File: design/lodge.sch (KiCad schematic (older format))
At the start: 12 parts

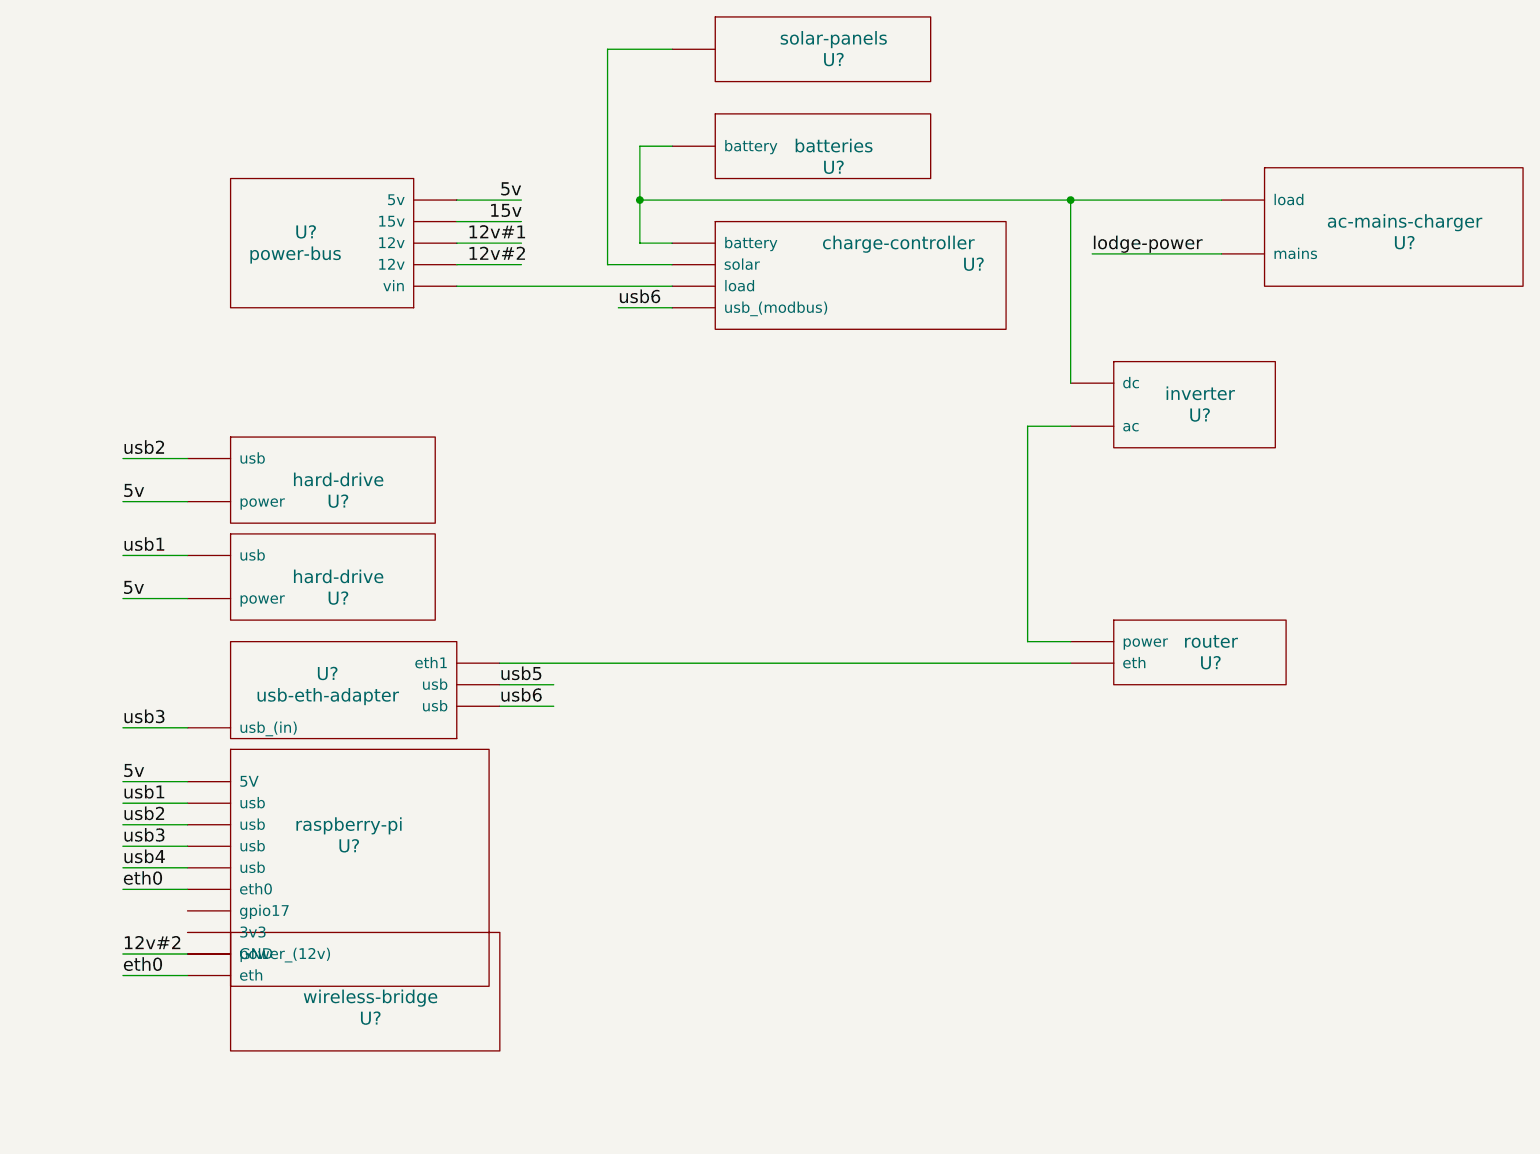
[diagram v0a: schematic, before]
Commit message: Hide component references.
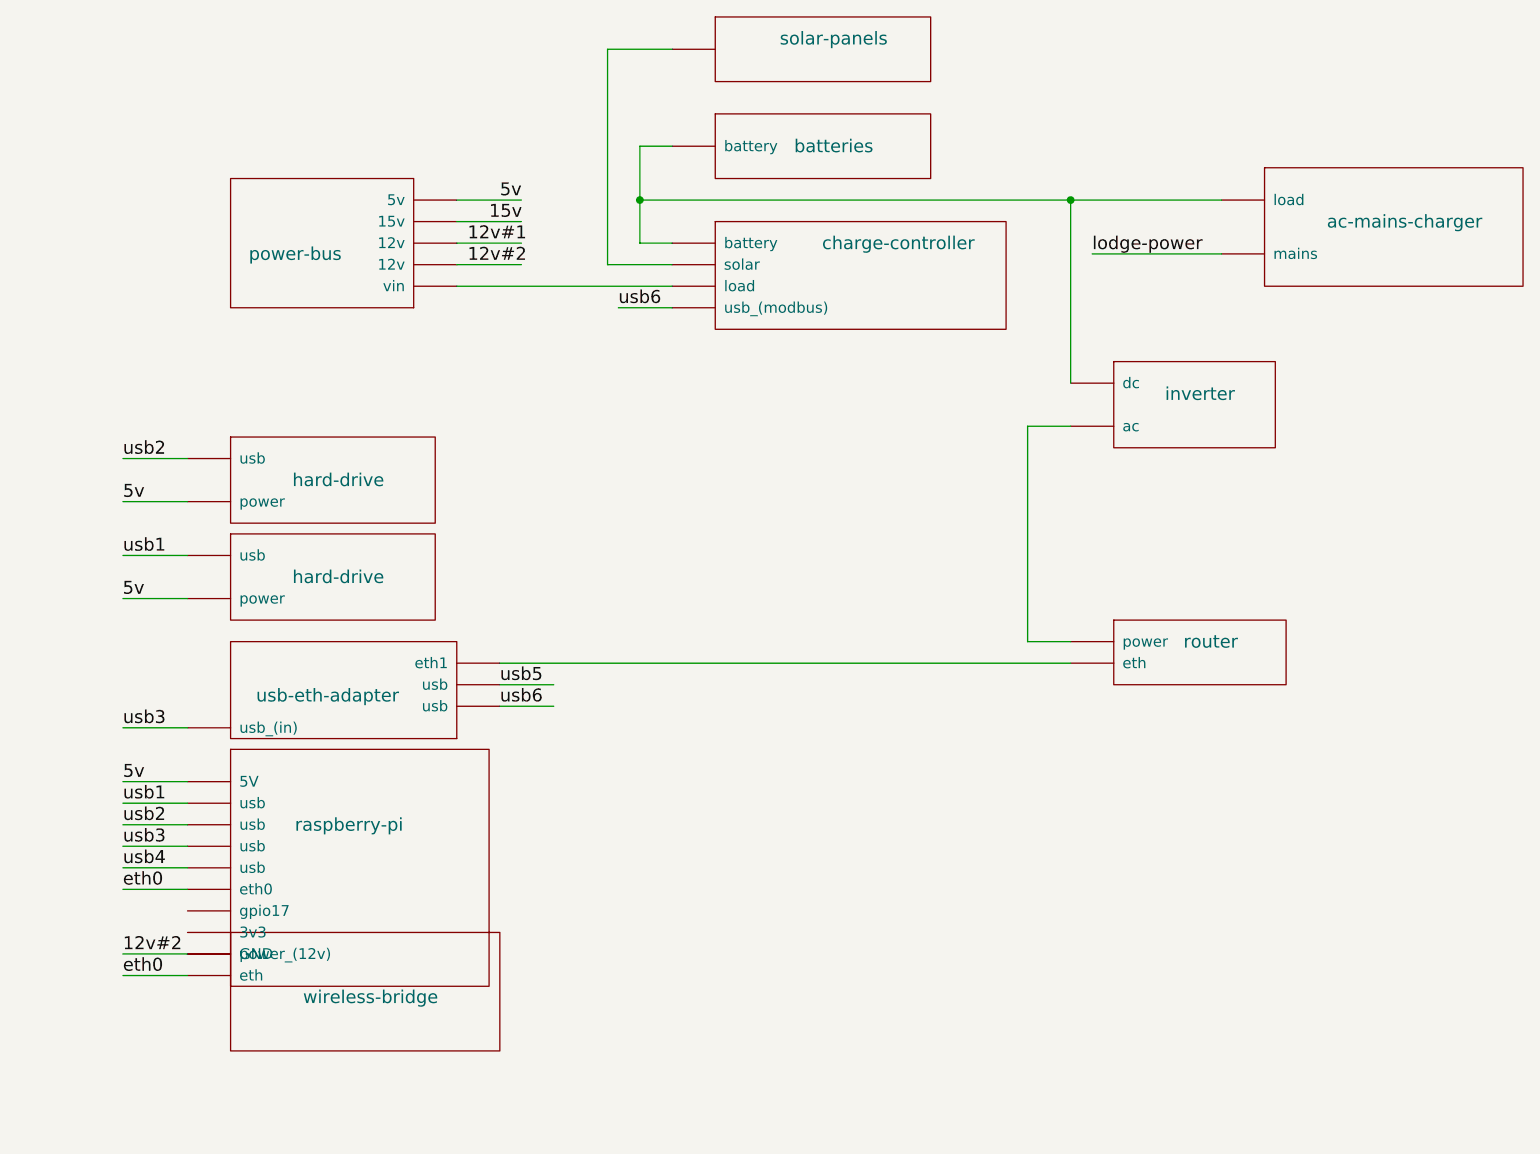
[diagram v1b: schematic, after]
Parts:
- gave numbers to parts that had none: 12
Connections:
- wire segments 36 -> 34
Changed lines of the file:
@@
 LIBS:valves
 LIBS:high-level
+LIBS:design-cache
 EELAYER 25 0
 EELAYER END
@@
 $EndDescr
 $Comp
-L charge-controller U?
+L charge-controller U23
 U 1 1 593F5FDD
 P 6750 2600
-F 0 "U?" H 6900 2700 60  0000 C CNN
+F 0 "U23" H 6900 2700 60  0001 C CNN
 F 1 "charge-controller" H 6550 2800 60  0000 C CNN
 F 2 "" H 6750 2600 60  0001 C CNN
@@
 $EndComp
 $Comp
-L power-bus U?
+L power-bus U15
 U 1 1 593F5FEB
 P 3750 2450
-F 0 "U?" H 3700 2350 60  0000 C CNN
+F 0 "U15" H 3700 2350 60  0001 C CNN
 F 1 "power-bus" H 3750 2450 60  0000 C CNN
 F 2 "" H 3750 2450 60  0001 C CNN
@@
 $EndComp
 $Comp
-L raspberry-pi U?
+L raspberry-pi U19
 U 1 1 593F5FF2
 P 4000 5100
-F 0 "U?" H 4000 5000 60  0000 C CNN
+F 0 "U19" H 4000 5000 60  0001 C CNN
 F 1 "raspberry-pi" H 4000 5100 60  0000 C CNN
 F 2 "" H 4000 5100 60  0001 C CNN
@@
 $EndComp
 $Comp
-L usb-eth-adapter U?
+L usb-eth-adapter U16
 U 1 1 593F5FF9
 P 3900 4500
-F 0 "U?" H 3900 4400 60  0000 C CNN
+F 0 "U16" H 3900 4400 60  0001 C CNN
 F 1 "usb-eth-adapter" H 3900 4500 60  0000 C CNN
 F 2 "" H 3900 4500 60  0001 C CNN
@@
 $EndComp
 $Comp
-L wireless-bridge U?
+L wireless-bridge U20
 U 1 1 593F6000
 P 4100 5900
-F 0 "U?" H 4100 5800 60  0000 C CNN
+F 0 "U20" H 4100 5800 60  0001 C CNN
 F 1 "wireless-bridge" H 4100 5900 60  0000 C CNN
 F 2 "" H 4100 5900 60  0001 C CNN
@@
 $EndComp
 $Comp
-L hard-drive U?
+L hard-drive U18
 U 1 1 593F6007
 P 3950 3950
-F 0 "U?" H 3950 3850 60  0000 C CNN
+F 0 "U18" H 3950 3850 60  0001 C CNN
 F 1 "hard-drive" H 3950 3950 60  0000 C CNN
 F 2 "" H 3950 3950 60  0001 C CNN
@@
 $EndComp
 $Comp
-L hard-drive U?
+L hard-drive U17
 U 1 1 593F600E
 P 3950 3500
-F 0 "U?" H 3950 3400 60  0000 C CNN
+F 0 "U17" H 3950 3400 60  0001 C CNN
 F 1 "hard-drive" H 3950 3500 60  0000 C CNN
 F 2 "" H 3950 3500 60  0001 C CNN
@@
 12v#2
 $Comp
-L batteries U?
+L batteries U22
 U 1 1 593F601A
 P 6250 1950
-F 0 "U?" H 6250 1850 60  0000 C CNN
+F 0 "U22" H 6250 1850 60  0001 C CNN
 F 1 "batteries" H 6250 1950 60  0000 C CNN
 F 2 "" H 6250 1950 60  0001 C CNN
@@
 	5350 2400 5500 2400
 Wire Wire Line
-	5350 1950 5350 2200
-Wire Wire Line
-	5350 2200 5350 2400
+	5350 1950 5350 2400
 Wire Wire Line
 	5350 1950 5500 1950
@@
 	5250 2700 5500 2700
 $Comp
-L solar-panels U?
+L solar-panels U21
 U 1 1 593F606C
 P 6250 1500
-F 0 "U?" H 6250 1450 60  0000 C CNN
+F 0 "U21" H 6250 1450 60  0001 C CNN
 F 1 "solar-panels" H 6250 1550 60  0000 C CNN
 F 2 "" H 6250 1550 60  0001 C CNN
@@
 	5200 1500 5500 1500
 $Comp
-L ac-mains-charger U?
+L ac-mains-charger U26
 U 1 1 593F63BD
 P 8900 2300
-F 0 "U?" H 8900 2200 60  0000 C CNN
+F 0 "U26" H 8900 2200 60  0001 C CNN
 F 1 "ac-mains-charger" H 8900 2300 60  0000 C CNN
 F 2 "" H 8900 2300 60  0001 C CNN
@@
 $EndComp
 $Comp
-L inverter U?
+L inverter U24
 U 1 1 593F6430
 P 7950 3150
-F 0 "U?" H 7950 3100 60  0000 C CNN
+F 0 "U24" H 7950 3100 60  0001 C CNN
 F 1 "inverter" H 7950 3200 60  0000 C CNN
 F 2 "" H 7950 3200 60  0001 C CNN
@@
 $EndComp
 $Comp
-L router U?
+L router U25
 U 1 1 593F66CA
 P 8000 4300
-F 0 "U?" H 8000 4250 60  0000 C CNN
+F 0 "U25" H 8000 4250 60  0001 C CNN
 F 1 "router" H 8000 4350 60  0000 C CNN
 F 2 "" H 8000 4350 60  0001 C CNN
@@
 $EndComp
 Wire Wire Line
-	5350 2200 7350 2200
-Wire Wire Line
-	7350 2200 8050 2200
+	5350 2200 8050 2200
 Wire Wire Line
 	7350 2200 7350 3050

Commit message: Updating hardware design docs.
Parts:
- removed U17: hard-drive, symbol hard-drive
- added U?: relay-board, symbol relay-board
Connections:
- net labels added: +3V3, GND, relay_en
- net labels removed: 12v#1, 15v
- wire segments 34 -> 39
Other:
- note added: "5v: 5v @ 3A\n12v#2: 12v @ 4.2A"
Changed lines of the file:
@@
 L raspberry-pi U19
 U 1 1 593F5FF2
-P 4000 5100
-F 0 "U19" H 4000 5000 60  0001 C CNN
-F 1 "raspberry-pi" H 4000 5100 60  0000 C CNN
-F 2 "" H 4000 5100 60  0001 C CNN
-F 3 "" H 4000 5100 60  0001 C CNN
-	1    4000 5100
+P 4000 5150
+F 0 "U19" H 4000 5050 60  0001 C CNN
+F 1 "raspberry-pi" H 4000 5150 60  0000 C CNN
+F 2 "" H 4000 5150 60  0001 C CNN
+F 3 "" H 4000 5150 60  0001 C CNN
+	1    4000 5150
 	1    0    0    -1
 $EndComp
@@
 L wireless-bridge U20
 U 1 1 593F6000
-P 4100 5900
-F 0 "U20" H 4100 5800 60  0001 C CNN
-F 1 "wireless-bridge" H 4100 5900 60  0000 C CNN
-F 2 "" H 4100 5900 60  0001 C CNN
-F 3 "" H 4100 5900 60  0001 C CNN
-	1    4100 5900
+P 4100 6300
+F 0 "U20" H 4100 6200 60  0001 C CNN
+F 1 "wireless-bridge" H 4100 6300 60  0000 C CNN
+F 2 "" H 4100 6300 60  0001 C CNN
+F 3 "" H 4100 6300 60  0001 C CNN
+	1    4100 6300
 	1    0    0    -1
 $EndComp
@@
 	1    0    0    -1
 $EndComp
-$Comp
-L hard-drive U17
-U 1 1 593F600E
-P 3950 3500
-F 0 "U17" H 3950 3400 60  0001 C CNN
-F 1 "hard-drive" H 3950 3500 60  0000 C CNN
-F 2 "" H 3950 3500 60  0001 C CNN
-F 3 "" H 3950 3500 60  0001 C CNN
-	1    3950 3500
-	1    0    0    -1
-$EndComp
 Text Label 4700 2200 0    60   ~ 0
 5v
-Text Label 4650 2300 0    60   ~ 0
-15v
-Text Label 4550 2400 0    60   ~ 0
-12v#1
 Text Label 4550 2500 0    60   ~ 0
 12v#2
@@
 	1    0    0    -1
 $EndComp
-Text Label 2950 4900 0    60   ~ 0
+Text Label 2950 4950 0    60   ~ 0
 5v
 Wire Wire Line
-	2950 5800 3250 5800
+	2950 6200 3250 6200
 Wire Wire Line
 	4700 4350 7350 4350
@@
 	4500 2200 4800 2200
 Wire Wire Line
-	4800 2300 4500 2300
-Wire Wire Line
-	4800 2400 4500 2400
-Wire Wire Line
 	4800 2500 4500 2500
 Wire Wire Line
@@
 	5350 1950 5500 1950
 Wire Wire Line
-	2950 4900 3250 4900
-Wire Wire Line
-	2950 5000 3250 5000
-Wire Wire Line
-	2950 5100 3250 5100
-Wire Wire Line
-	2950 5200 3250 5200
-Wire Wire Line
-	2950 5300 3250 5300
-Text Label 2950 5000 0    60   ~ 0
+	2950 4950 3250 4950
+Wire Wire Line
+	2950 5050 3250 5050
+Wire Wire Line
+	2950 5150 3250 5150
+Wire Wire Line
+	2950 5250 3250 5250
+Wire Wire Line
+	2950 5350 3250 5350
+Text Label 2950 5050 0    60   ~ 0
 usb1
-Text Label 2950 5100 0    60   ~ 0
+Text Label 2950 5150 0    60   ~ 0
 usb2
-Text Label 2950 5200 0    60   ~ 0
+Text Label 2950 5250 0    60   ~ 0
 usb3
-Text Label 2950 5300 0    60   ~ 0
+Text Label 2950 5350 0    60   ~ 0
 usb4
 Wire Wire Line
@@
 Wire Wire Line
 	2950 4050 3250 4050
-Wire Wire Line
-	2950 3600 3250 3600
-Wire Wire Line
-	2950 3400 3250 3400
 Text Label 3050 4050 2    60   ~ 0
 5v
-Text Label 2950 3600 0    60   ~ 0
-5v
-Text Label 2950 3400 0    60   ~ 0
-usb2
 Text Label 2950 3850 0    60   ~ 0
 usb1
@@
 	2950 4650 3250 4650
 Wire Wire Line
-	3250 5400 2950 5400
-Text Label 2950 5400 0    60   ~ 0
+	3250 5450 2950 5450
+Text Label 2950 5450 0    60   ~ 0
 eth0
-Text Label 2950 5800 0    60   ~ 0
+Text Label 2950 6200 0    60   ~ 0
 eth0
 Wire Wire Line
-	3250 5700 2950 5700
-Text Label 2950 5700 0    60   ~ 0
+	3250 6100 2950 6100
+Text Label 2950 6100 0    60   ~ 0
 12v#2
 Text Label 4700 4450 0    60   ~ 0
@@
 L inverter U24
 U 1 1 593F6430
-P 7950 3150
-F 0 "U24" H 7950 3100 60  0001 C CNN
-F 1 "inverter" H 7950 3200 60  0000 C CNN
-F 2 "" H 7950 3200 60  0001 C CNN
-F 3 "" H 7950 3200 60  0001 C CNN
-	1    7950 3150
+P 7950 3800
+F 0 "U24" H 7950 3750 60  0001 C CNN
+F 1 "inverter" H 7950 3850 60  0000 C CNN
+F 2 "" H 7950 3850 60  0001 C CNN
+F 3 "" H 7950 3850 60  0001 C CNN
+	1    7950 3800
 	1    0    0    -1
 $EndComp
@@
 	5350 2200 8050 2200
 Wire Wire Line
-	7350 2200 7350 3050
+	7350 2200 7350 3600
 Connection ~ 5350 2200
 Connection ~ 7350 2200
-Wire Wire Line
-	7150 3250 7150 4250
-Wire Wire Line
-	7150 3250 7350 3250
 Wire Wire Line
 	7150 4250 7350 4250
@@
 Text Label 7450 2450 0    60   ~ 0
 lodge-power
+Text Notes 2500 2400 0    60   ~ 0
+5v:     5v @ 3A\n12v#2: 12v @ 4.2A
+$Comp
+L relay-board U?
+U 1 1 5A146A14
+P 6400 3600
+F 0 "U?" H 6400 3600 60  0000 C CNN
+F 1 "relay-board" H 6400 3500 60  0000 C CNN
+F 2 "" H 6400 3600 60  0001 C CNN
+F 3 "" H 6400 3600 60  0001 C CNN
+	1    6400 3600
+	1    0    0    -1
+$EndComp
+Wire Wire Line
+	7050 3700 7350 3700
+Wire Wire Line
+	7350 3600 7050 3600
+Wire Wire Line
+	5250 3800 5700 3800
+Wire Wire Line
+	5250 3700 5700 3700
+Wire Wire Line
+	5250 3600 5700 3600
+$Comp
+L GND #PWR?
+U 1 1 5A146CDD
+P 5250 3700
+F 0 "#PWR?" H 5250 3450 50  0001 C CNN
+F 1 "GND" H 5250 3550 50  0000 C CNN
+F 2 "" H 5250 3700 50  0001 C CNN
+F 3 "" H 5250 3700 50  0001 C CNN
+	1    5250 3700
+	0    1    1    0
+$EndComp
+$Comp
+L GND #PWR?
+U 1 1 5A146D00
+P 3000 5750
+F 0 "#PWR?" H 3000 5500 50  0001 C CNN
+F 1 "GND" H 3000 5600 50  0000 C CNN
+F 2 "" H 3000 5750 50  0001 C CNN
+F 3 "" H 3000 5750 50  0001 C CNN
+	1    3000 5750
+	0    1    1    0
+$EndComp
+$Comp
+L +3V3 #PWR?
+U 1 1 5A146D0F
+P 5250 3550
+F 0 "#PWR?" H 5250 3400 50  0001 C CNN
+F 1 "+3V3" H 5250 3690 50  0000 C CNN
+F 2 "" H 5250 3550 50  0001 C CNN
+F 3 "" H 5250 3550 50  0001 C CNN
+	1    5250 3550
+	1    0    0    -1
+$EndComp
+$Comp
+L +3V3 #PWR?
+U 1 1 5A146D24
+P 2650 5650
+F 0 "#PWR?" H 2650 5500 50  0001 C CNN
+F 1 "+3V3" H 2650 5790 50  0000 C CNN
+F 2 "" H 2650 5650 50  0001 C CNN
+F 3 "" H 2650 5650 50  0001 C CNN
+	1    2650 5650
+	0    -1   -1   0
+$EndComp
+Text Label 2950 5550 0    60   ~ 0
+relay_en
+Wire Wire Line
+	3250 5550 2950 5550
+Wire Wire Line
+	2650 5650 3250 5650
+Wire Wire Line
+	3250 5750 3000 5750
+Wire Wire Line
+	5250 3600 5250 3550
+Text Label 5250 3800 0    60   ~ 0
+relay_en
+Wire Wire Line
+	7350 3900 7150 3900
+Wire Wire Line
+	7150 3900 7150 4250
 $EndSCHEMATC
